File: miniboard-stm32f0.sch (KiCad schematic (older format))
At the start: 1 part

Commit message: 1st version
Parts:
- added C1, C2, C3: 20pF, Capacitors_SMD:C_0603, symbol C
- added H1, H2, H3, H4: HOLE, mechanics:hole_2mm, symbol HOLE
- added P1, P_BOOT0, P_POWER1: CONN_01X02, Pin_Headers:Pin_Header_Straight_1x02, symbol CONN_01X02
- added P2: CONN_01X13, Pin_Headers:Pin_Header_Straight_1x13, symbol CONN_01X13
- added P3: CONN_01X01, Pin_Headers:Pin_Header_Straight_1x01, symbol CONN_01X01
- added P_POWER_BOARD1: CONN_01X03, Pin_Headers:Pin_Header_Straight_1x03, symbol CONN_01X03
- added P_SWD1, P_UART1: CONN_01X04, Pin_Headers:Pin_Header_Straight_1x04, symbol CONN_01X04
- added R1, R2: 4.7k, Resistors_SMD:R_0603, symbol R
- added SW1, SW2: SW_PUSH, Buttons_Switches_SMD:SW_SPST_EVQP2, symbol SW_PUSH
- added Y1: 8MHz, Crystals:crystal_FA238-TSX3225, symbol Crystal
- U1: renamed from U?; footprint (none) -> tssop:tssop20
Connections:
- net BOOT0: now reaches U1.1 (BOOT0)
- net BOOT0: now also P_BOOT0.1 (P1), R1.2
- net PA4: now reaches U1.10 (PA4)
- net PA4: now also P2.5 (P5)
- net PA5: now reaches U1.11 (PA5)
- net PA5: now also P2.6 (P6)
- net PA6: now reaches U1.12 (PA6)
- net PA6: now also P2.7 (P7)
- net PA7: now reaches U1.13 (PA7)
- net PA7: now also P2.8 (P8)
- net PB1: now reaches U1.14 (PB1)
- net PB1: now also P2.9 (P9)
- net GND: now reaches U1.15 (VSS)
- net GND: now also C1.2, C2.2, C3.2, P3.1 (P1), P_BOOT0.2 (P2), P_POWER1.2 (P2), P_POWER_BOARD1.3 (P3), P_SWD1.4 (P4), P_UART1.4 (P4), SW1.1, SW2.1
- net +3V3: now reaches U1.16 (VDD)
- net +3V3: now also P1.1 (P1), P_POWER1.1 (P1), P_POWER_BOARD1.1 (P1), P_SWD1.1 (P1), P_UART1.1 (P1), R1.1, R2.1
- net PA9_TX: now reaches U1.17 (PA9)
- net PA9_TX: now also P2.10 (P10), P_UART1.3 (P3)
- net PA10_RX: now reaches U1.18 (PA10)
- net PA10_RX: now also P2.11 (P11), P_UART1.2 (P2)
- net PA13_SWDIO: now reaches U1.19 (PA13)
- net PA13_SWDIO: now also P2.12 (P12), P_SWD1.2 (P2)
- net OSC_IN: now reaches U1.2 (OSC_IN)
- net OSC_IN: now also C1.1, Y1.1
- net PA14_SWCLK: now reaches U1.20 (PA14)
- net PA14_SWCLK: now also P2.13 (P13), P_SWD1.3 (P3)
- net OSC_OUT: now reaches U1.3 (OSC_OUT)
- net OSC_OUT: now also C2.1, Y1.2
- net NRST: now reaches U1.4 (NRST)
- net NRST: now also C3.1, R2.2, SW1.2, SW2.2
- net VAA: now reaches U1.5 (VDDA)
- net VAA: now also P1.2 (P2), P_POWER_BOARD1.2 (P2)
- net PA0: now reaches U1.6 (PA0)
- net PA0: now also P2.1 (P1)
- net PA1: now reaches U1.7 (PA1)
- net PA1: now also P2.2 (P2)
- net PA2: now reaches U1.8 (PA2)
- net PA2: now also P2.3 (P3)
- net PA3: now reaches U1.9 (PA3)
- net PA3: now also P2.4 (P4)
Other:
- note added: "2 switches\n1 footprint on each side \nof the board"
- note added: "Jumper ON : boot from flash\nJumper OFF : boot from memory"
- moved on the sheet: U1

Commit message: Change quartz footprint, add text
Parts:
- Y1: footprint Crystals:crystal_FA238-TSX3225 -> Crystals:Crystal_HC49-U_Vertical
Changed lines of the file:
@@
 F 0 "Y1" H 2400 6350 50  0000 C CNN
 F 1 "8MHz" H 2400 6050 50  0000 C CNN
-F 2 "Crystals:crystal_FA238-TSX3225" H 2400 6200 60  0001 C CNN
+F 2 "Crystals:Crystal_HC49-U_Vertical" H 2400 6200 60  0001 C CNN
 F 3 "" H 2400 6200 60  0000 C CNN
 	1    2400 6200

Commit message: * Use edge connector for SWD and uart connector * Add power LED * Fix reset button footprint * Add decoupling caps * Realign power connector
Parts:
- removed P2: CONN_01X13, Pin_Headers:Pin_Header_Straight_1x13, symbol CONN_01X13
- removed P_SWD1, P_UART1: CONN_01X04, Pin_Headers:Pin_Header_Straight_1x04, symbol CONN_01X04
- added C4: 4.7uF, Capacitors_Tantalum_SMD:TantalC_SizeR_EIA-2012, symbol CP
- added C5: 100pF, Capacitors_SMD:C_0603, symbol C
- added C6: 1uF, Capacitors_Tantalum_SMD:TantalC_SizeR_EIA-2012, symbol CP
- added C7: 10pF, Capacitors_SMD:C_0603, symbol C
- added D1, D2: LED, Diodes_SMD:SOD-123, symbol LED
- added P2: CONN_01X11, Pin_Headers:Pin_Header_Straight_1x11, symbol CONN_01X11
- added P4: CONN_02X03, edge_connectors:pin_header_edge_6, symbol CONN_02X03
- added R3: 4.7k, Resistors_SMD:R_0603, symbol R
- H1, H2, H3, H4: footprint mechanics:hole_2mm -> mechanics:hole_2.5mm
- SW1, SW2: footprint Buttons_Switches_SMD:SW_SPST_EVQP2 -> Buttons_Switches_SMD:SW_SPST_EVQQ2
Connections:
- net +3V3: now also C4.1, C5.1, P4.2 (P2), R3.1
- net GND: now also H1.1, H2.1, H3.1, H4.1, C4.2, C5.2, C6.2, C7.2, D1.1 (K), D2.1 (K), P4.1 (P1)
- net PA0: now also P2.1 (P1)
- net PA1: now also P2.2 (P2)
- net PA10_RX: now also P2.11 (P11), P4.4 (P4)
- net PA13_SWDIO: now also P4.3 (P3)
- net PA14_SWCLK: now also P4.5 (P5)
- net PA2: now also P2.3 (P3)
- net PA3: now also P2.4 (P4)
- net PA4: now also P2.5 (P5)
- net PA5: now also P2.6 (P6)
- net PA6: now also P2.7 (P7)
- net PA7: now also P2.8 (P8)
- net PA9_TX: now also P2.10 (P10), P4.6 (P6)
- net PB1: now also P2.9 (P9)
- net VAA: now also C6.1, C7.1
- new net: D1.2 (A), D2.2 (A), R3.2
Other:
- note added: "Programming port : swdio / uart"
- note added: "VDD decoupling"
- note added: "VDDA decoupling"

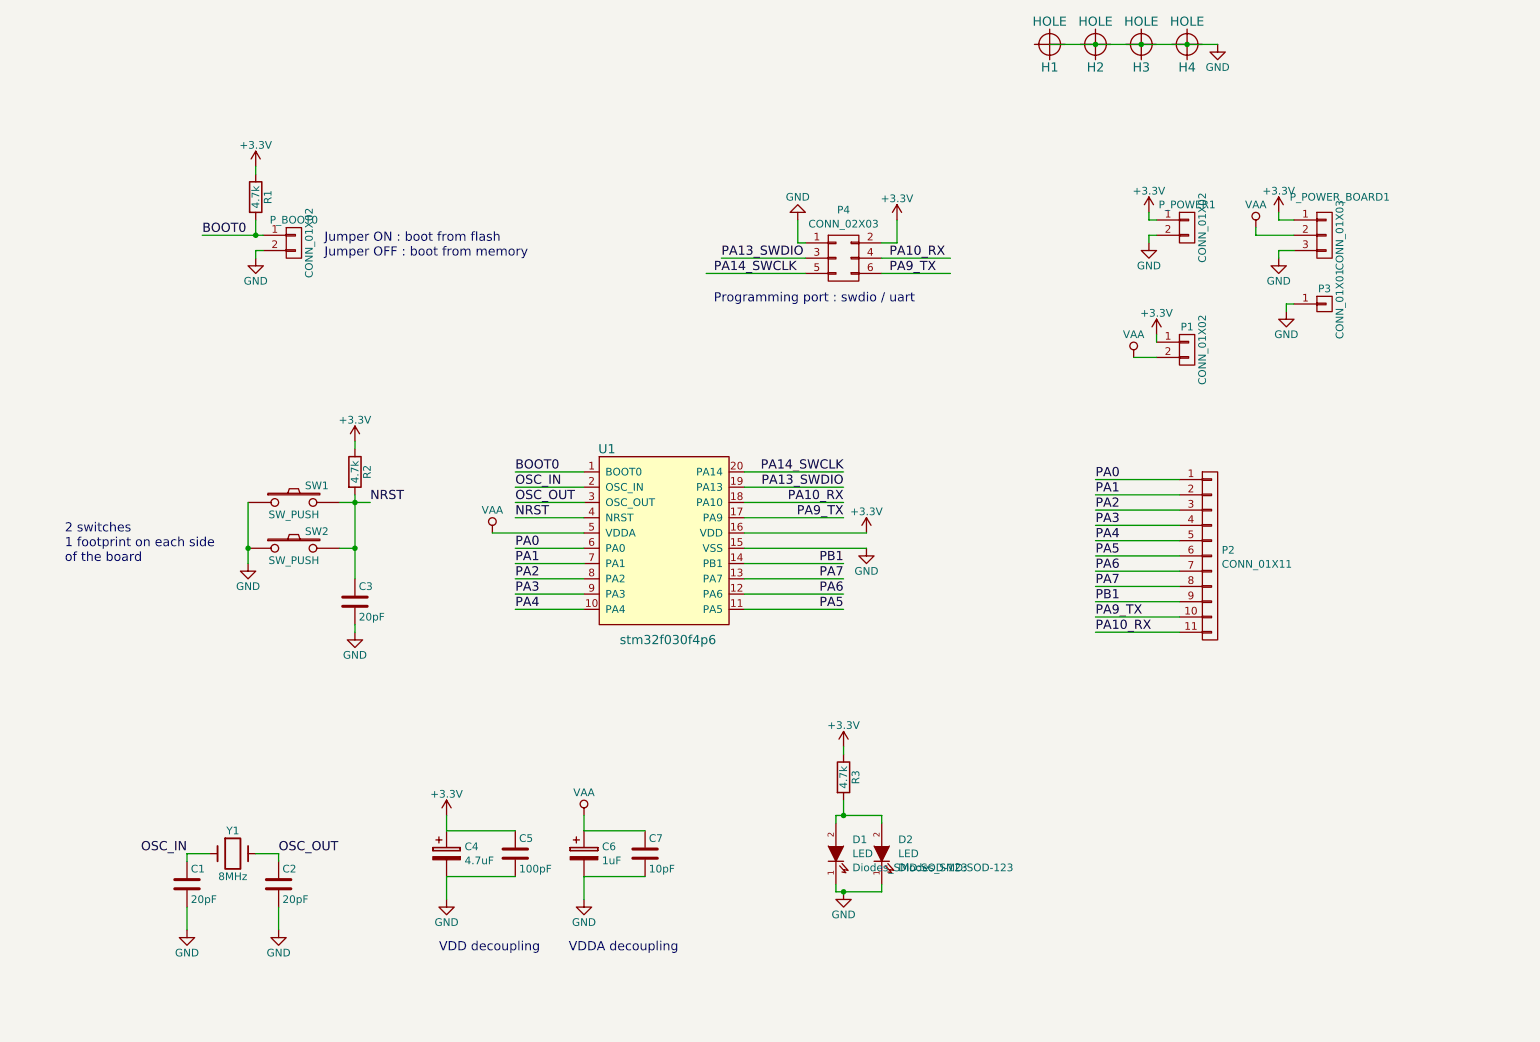
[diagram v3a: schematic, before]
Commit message: Fix minor routing issues Redraw mask
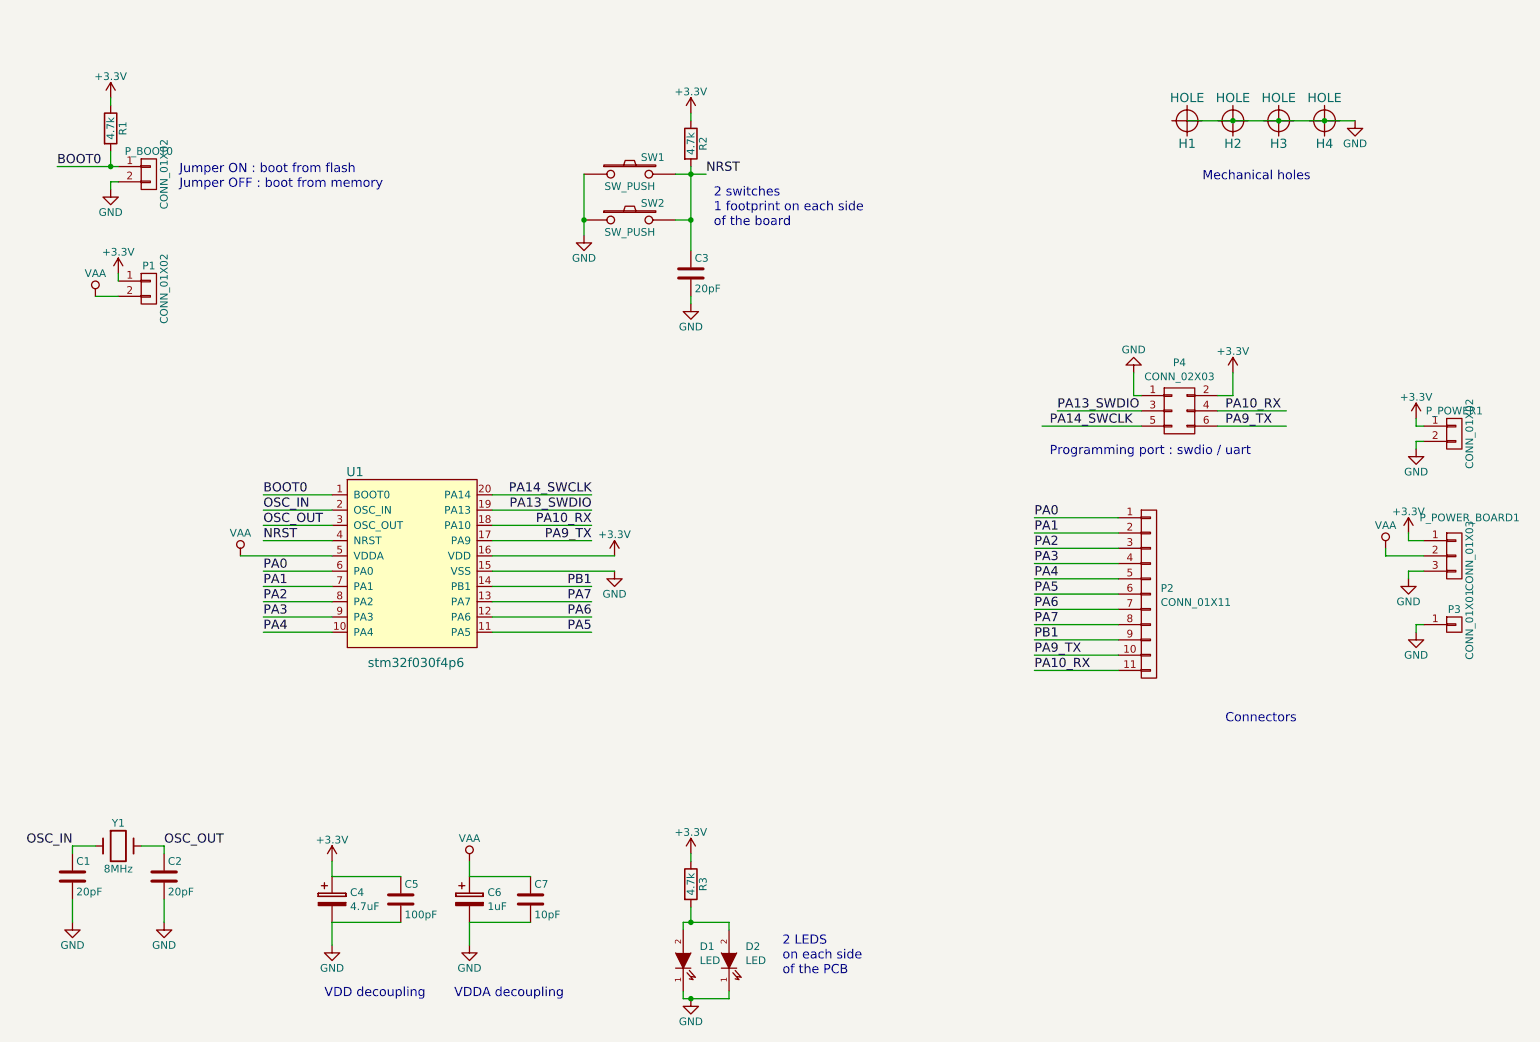
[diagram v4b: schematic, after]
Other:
- note added: "2 LEDS\non each side \nof the PCB"
- note added: "Connectors"
- note added: "Mechanical holes"
- moved on the sheet: C1, C2, C3, C4, C5, C6, C7, D1, D2, H1, H2, H3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
